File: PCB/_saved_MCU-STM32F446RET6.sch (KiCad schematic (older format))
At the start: 48 parts, among them J3 20021121-00010C4LF, J4 0475890001-MicroUSBPort, P1 CONN_01X20, P2 CONN_01X20, SW1 B3U-1000P, U3 STM32F446RET6_-_TQFP64, X1 ABM3B8.000MHZB2T, X2 ABS07-32.768KHZ-9-T

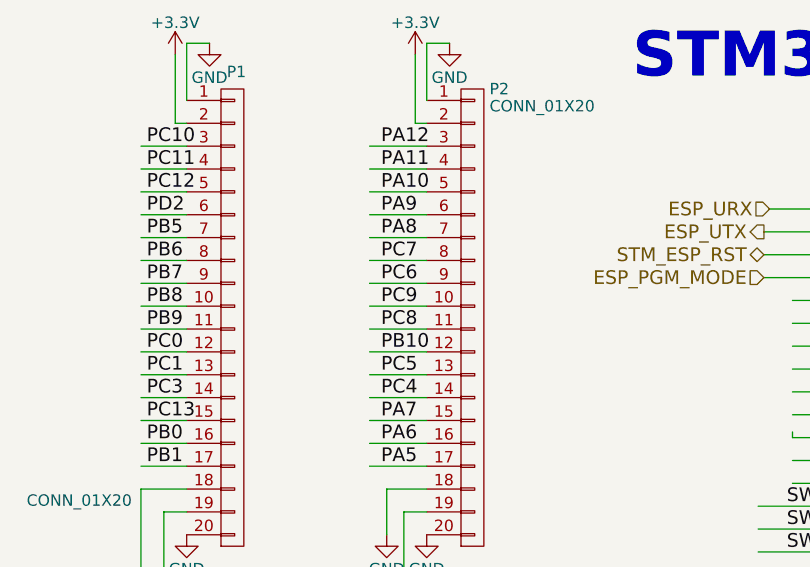
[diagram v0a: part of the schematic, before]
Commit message: Layout
layout underway, one side completely routed, next other side, ESP, and
PCB antenna. Added PDF for app not on 2.4GHZ antenna similar to the one
sparkfun uses in their thing boards, I suspect this is where they got it
and it seems reliable.
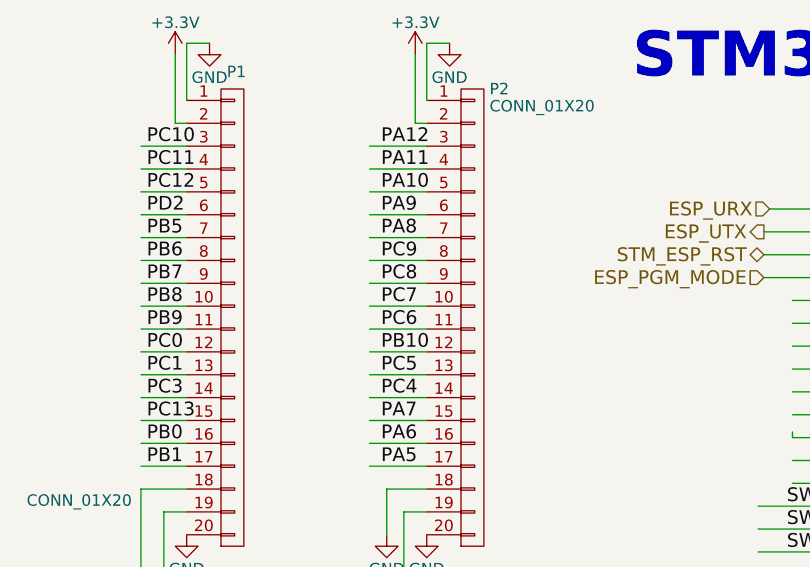
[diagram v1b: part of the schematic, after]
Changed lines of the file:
@@
 Wire Wire Line
 	2450 1975 2200 1975
-Text Label 2250 1775 0    60   ~ 0
+Text Label 2250 1975 0    60   ~ 0
 PC6
-Text Label 2250 1675 0    60   ~ 0
+Text Label 2250 1875 0    60   ~ 0
 PC7
 Wire Wire Line
@@
 Wire Wire Line
 	2200 1775 2450 1775
-Text Label 2250 1875 0    60   ~ 0
+Text Label 2250 1675 0    60   ~ 0
 PC9
-Text Label 2250 1975 0    60   ~ 0
+Text Label 2250 1775 0    60   ~ 0
 PC8
 Wire Wire Line
